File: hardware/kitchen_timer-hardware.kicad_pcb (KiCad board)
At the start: 2 copper layers, 60 x 110.8 mm, 80 parts, among them J1 Conn_01x02, J2 Conn_01x02_Pin, J3 AVR-ISP-6, Q1 JSM2302, Q2 IRLML6402, Q3 MMBT3904, SW2 SKRPACE010, U1 CH340E UART Module, U10 MAX7219, U11 KWM-20882CUYB, U12 KWM-20882CUYB, U13 KWM-20882CUYB, U14 KWM-20882CUYB, U2 TP4056 breakout, U3 SparkFun_LiPower, U5 ATMEGA328P-AU, U6 PEC11R-4215F-S0024, U7 MAX7219, U8 MAX7219, U9 MAX7219, Y1 Crystal-32kHz

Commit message: Add description text
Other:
- board text added: "Kitchen Timer V1 2025-05-12 Nicolas Perozzi, Erasmus Cedernaes"
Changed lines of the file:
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@@
 		(layer "User.1")
+	)
+	(gr_text "Kitchen Timer V1\n2025-05-12\nNicolas Perozzi, Erasmus Cedernaes"
+		(at 135.5744 64.7192 90)
+		(layer "B.SilkS")
+		(effects
+			(font
+				(size 1 1.016)
+				(thickness 0.195)
+				(bold yes)
+			)
+			(justify left bottom mirror)
+		)
 	)
 	(segment

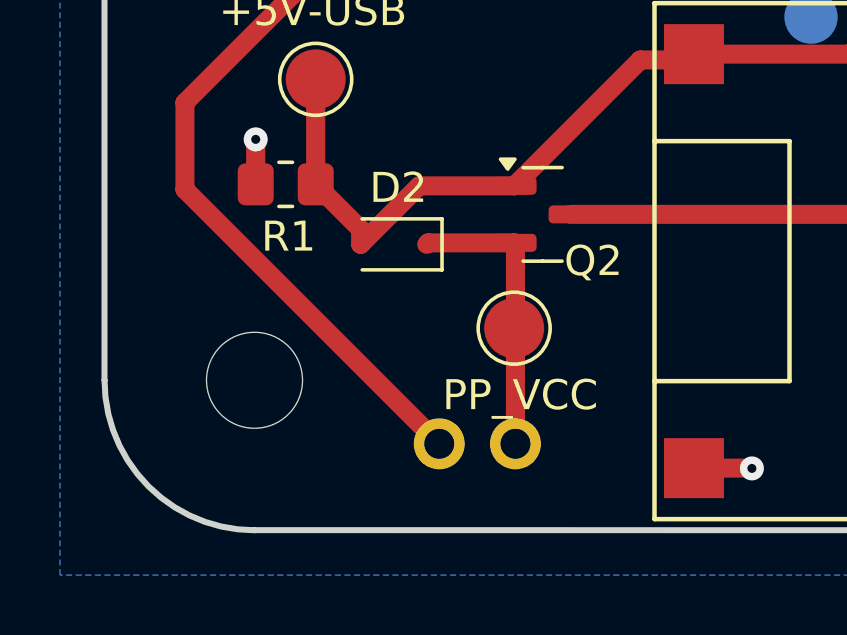
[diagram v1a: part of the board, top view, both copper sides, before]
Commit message: Move J2 connector further from the edge
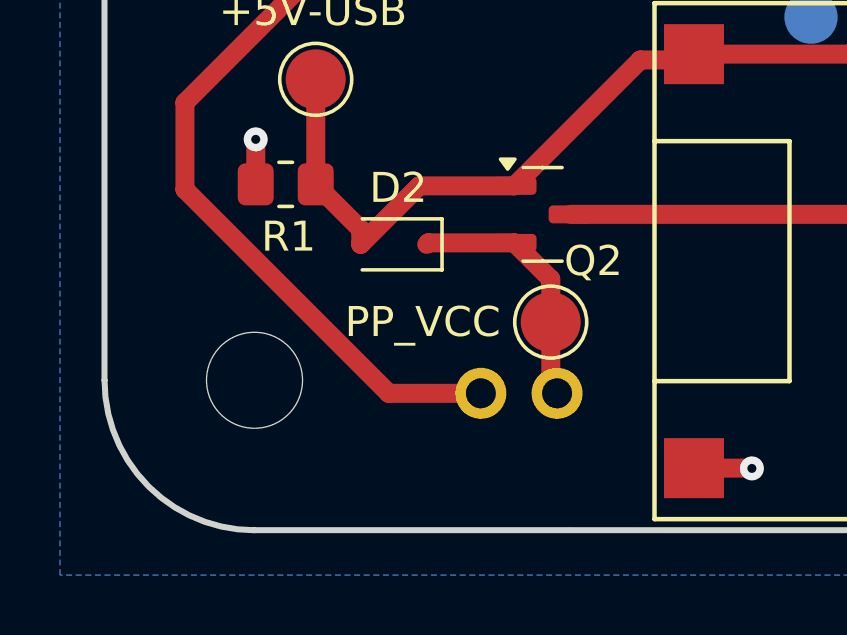
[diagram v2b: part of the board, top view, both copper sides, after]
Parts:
- moved J2 2.18 mm to (144.5, 136.4)
- moved TP13 1.24 mm to (141.9, 131.8)
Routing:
- net /+5V Boost Converter/PP_VCC: track 9.66 -> 8.55 mm
- net /+5V Boost Converter/PP_VCC_after_switch: track 25.8 -> 26.4 mm
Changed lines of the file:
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@@
 	(footprint "TestPoint:TestPoint_Pad_D2.0mm"
 		(layer "F.Cu")
-		(at 140.6544 131.9784)
+		(at 141.8736 131.7752)
 		(descr "SMD pad as test Point, diameter 2.0mm")
 		(tags "test point SMD pad")
@@
 		)
 		(property "Value" "PP_VCC"
-			(at 0.2032 2.2352 0)
+			(at -4.2672 0 0)
 			(layer "F.SilkS")
 			(effects
@@
 	(footprint "kitchen_timer:JST_XH_1x02_P2.54mm_Vertical"
 		(layer "B.Cu")
-		(at 143.1277 138.1321 180)
+		(at 144.5152 136.4488 180)
 		(descr "JST XH series connector, B2B-XH-AM, with boss (http://www.jst-mfg.com/product/pdf/eng/eXH.pdf), generated with kicad-footprint-generator")
 		(tags "connector JST XH vertical boss")
@@
 	)
 	(segment
-		(start 140.6977 129.1667)
+		(start 141.8736 133.9372)
+		(end 142.0852 134.1488)
+		(width 0.635)
+		(layer "F.Cu")
+		(net 12)
+	)
+	(segment
+		(start 141.8736 130.3426)
 		(end 140.665 129.134)
 		(width 0.635)
@@
 	)
 	(segment
-		(start 140.6977 135.8321)
-		(end 140.6977 129.1667)
+		(start 141.8736 131.7752)
+		(end 141.8736 130.3426)
 		(width 0.635)
 		(layer "F.Cu")
@@
 	)
 	(segment
+		(start 141.8736 131.7752)
+		(end 141.8736 133.9372)
+		(width 0.635)
+		(layer "F.Cu")
+		(net 12)
+	)
+	(segment
 		(start 140.665 129.134)
 		(end 137.79 129.134)
@@
 	)
 	(segment
+		(start 129.6816 124.46)
+		(end 136.9576 117.184)
+		(width 0.635)
+		(layer "F.Cu")
+		(net 22)
+	)
+	(segment
 		(start 136.9576 117.184)
 		(end 137.54 117.184)
@@
 	)
 	(segment
-		(start 129.6816 124.46)
-		(end 136.9576 117.184)
+		(start 139.5452 134.1488)
+		(end 136.4744 134.1488)
 		(width 0.635)
 		(layer "F.Cu")
@@
 	)
 	(segment
-		(start 138.1577 135.8321)
+		(start 136.4744 134.1488)
 		(end 129.6816 127.356)
 		(width 0.635)

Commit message: Run "cleanup tracks and vias"
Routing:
- net /LED Matrices Drivers/SCK: track 144.2 -> 143.1 mm
- net /Microcontroller/SW: track 12.0 -> 11.3 mm
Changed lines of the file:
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@@
 	)
 	(segment
-		(start 161.5775 76.184)
-		(end 161.54 76.184)
-		(width 0.2)
-		(layer "F.Cu")
-		(net 1)
-	)
-	(segment
 		(start 151.523 59.944)
 		(end 150.1032 59.944)
@@
 	(segment
 		(start 160.04 100.184)
-		(end 163.04 100.184)
+		(end 167.04 100.184)
 		(width 0.635)
 		(layer "F.Cu")
@@
 	(segment
 		(start 134.6854 77.184)
-		(end 134.6854 76.684)
+		(end 134.6854 74.8792)
 		(width 0.635)
 		(layer "F.Cu")
@@
 	(segment
 		(start 134.6854 97.3582)
-		(end 134.6854 89.184)
+		(end 134.6854 77.184)
 		(width 0.635)
 		(layer "F.Cu")
@@
 	)
 	(segment
-		(start 163.04 100.184)
-		(end 167.04 100.184)
-		(width 0.635)
-		(layer "F.Cu")
-		(net 2)
-	)
-	(segment
 		(start 137.54 89.184)
 		(end 139.54 87.184)
@@
 	)
 	(segment
-		(start 142.54 98.184)
-		(end 145.04 98.184)
+		(start 142.04 98.184)
+		(end 150.04 98.184)
 		(width 0.635)
 		(layer "F.Cu")
@@
 	)
 	(segment
-		(start 142.04 98.184)
-		(end 142.54 98.184)
-		(width 0.635)
-		(layer "F.Cu")
-		(net 2)
-	)
-	(segment
 		(start 135.7776 53.34)
 		(end 134.6865 52.2489)
@@
 	)
 	(segment
-		(start 134.6854 75.684)
-		(end 134.6854 74.8792)
-		(width 0.635)
-		(layer "F.Cu")
-		(net 2)
-	)
-	(segment
 		(start 158.0025 89.1465)
 		(end 158.54 89.1465)
@@
 	)
 	(segment
-		(start 134.6854 89.184)
-		(end 134.6854 77.184)
-		(width 0.635)
-		(layer "F.Cu")
-		(net 2)
-	)
-	(segment
 		(start 173.8024 109.4952)
 		(end 171.5248 109.4952)
@@
 	)
 	(segment
-		(start 159.5935 78.3917)
-		(end 159.54 78.4452)
-		(width 0.2)
-		(layer "F.Cu")
-		(net 2)
-	)
-	(segment
-		(start 134.6854 76.684)
-		(end 134.6854 75.684)
-		(width 0.635)
-		(layer "F.Cu")
-		(net 2)
-	)
-	(segment
 		(start 135.93 64.008)
 		(end 136.184 63.754)
@@
 	)
 	(segment
-		(start 145.04 98.184)
-		(end 150.04 98.184)
-		(width 0.635)
-		(layer "F.Cu")
-		(net 2)
-	)
-	(segment
 		(start 158.74 88.9465)
 		(end 158.54 89.1465)
@@
 	)
 	(segment
-		(start 142.54 85.1465)
+		(start 141.0775 85.1465)
 		(end 144.5775 85.1465)
 		(width 0.2)
@@
 		(net 5)
 	)
-	(segment
-		(start 141.0775 85.1465)
-		(end 142.54 85.1465)
-		(width 0.2)
-		(layer "F.Cu")
-		(net 5)
-	)
 	(via
 		(at 161.4824 86.5632)
@@
 	)
 	(segment
-		(start 157.54 93.684)
-		(end 157.04 93.184)
-		(width 0.2)
-		(layer "F.Cu")
-		(net 7)
-	)
-	(segment
 		(start 157.04 90.6465)
 		(end 155.54 89.1465)
@@
 	)
 	(segment
-		(start 146.54 97.835)
-		(end 146.54 97.184)
-		(width 0.2)
-		(layer "B.Cu")
-		(net 8)
-	)
-	(segment
 		(start 146.54 99.184)
-		(end 146.54 97.835)
+		(end 146.54 97.184)
 		(width 0.2)
 		(layer "B.Cu")
@@
 	)
 	(segment
-		(start 161.544 116.4105)
-		(end 161.544 116.188)
-		(width 0.2)
-		(layer "F.Cu")
-		(net 10)
-	)
-	(segment
 		(start 140.54 113.7792)
 		(end 143.7024 116.9416)
@@
 	)
 	(segment
-		(start 140.536592 99.1015)
-		(end 140.54 99.104908)
-		(width 0.2)
-		(layer "F.Cu")
-		(net 10)
-	)
-	(segment
 		(start 161.544 116.4105)
 		(end 161.8135 116.4105)
@@
 	)
 	(segment
-		(start 155.555525 121.684)
-		(end 155.54 121.684)
-		(width 0.2)
-		(layer "F.Cu")
-		(net 11)
-	)
-	(segment
-		(start 155.630125 121.6094)
-		(end 155.555525 121.684)
-		(width 0.2)
-		(layer "F.Cu")
-		(net 11)
-	)
-	(segment
 		(start 160.594 118.2855)
 		(end 159.3488 119.5307)
@@
 		(net 11)
 	)
-	(segment
-		(start 155.630125 121.6094)
-		(end 155.640329 121.599196)
-		(width 0.2)
-		(layer "F.Cu")
-		(net 11)
-	)
 	(via
 		(at 155.630125 121.6094)
@@
 		(net 13)
 	)
-	(segment
-		(start 153.04 121.659525)
-		(end 153.090125 121.6094)
-		(width 0.635)
-		(layer "F.Cu")
-		(net 13)
-	)
 	(via
 		(at 153.090125 121.6094)
@@
 		(net 23)
 	)
-	(segment
-		(start 161.79 80.6952)
-		(end 161.893124 80.592076)
-		(width 0.2)
-		(layer "F.Cu")
-		(net 23)
-	)
 	(via
 		(at 170.728 78.4194)
@@
 	)
 	(segment
-		(start 162.04 78.4452)
+		(start 160.34 78.4452)
 		(end 162.2788 78.4452)
 		(width 0.254)
@@
 	)
 	(segment
-		(start 160.34 78.4452)
-		(end 162.04 78.4452)
-		(width 0.254)
-		(layer "F.Cu")
-		(net 24)
-	)
-	(segment
 		(start 147.5968 36.508)
 		(end 146.9688 35.88)
@@
 	)
 	(segment
-		(start 176.651 81.295)
-		(end 177.2704 81.295)
-		(width 0.254)
-		(layer "F.Cu")
-		(net 24)
-	)
-	(segment
 		(start 137.588 37.377757)
 		(end 137.588 37.971615)
@@
 	)
 	(segment
-		(start 156.7072 56.1848)
-		(end 156.312 56.1848)
-		(width 0.254)
-		(layer "F.Cu")
-		(net 24)
-	)
-	(segment
 		(start 162.2788 78.4452)
 		(end 164.4288 78.4452)
@@
 	)
 	(segment
-		(start 141.540003 97.231203)
-		(end 141.54 97.2312)
-		(width 0.2)
-		(layer "F.Cu")
-		(net 28)
-	)
-	(segment
-		(start 153.3012 84.684)
-		(end 153.29 84.6952)
-		(width 0.2)
-		(layer "F.Cu")
-		(net 28)
-	)
-	(segment
 		(start 141.54 94.184)
 		(end 151.0288 84.6952)
@@
 	)
 	(segment
-		(start 141.536594 99.101499)
-		(end 141.54 99.104905)
-		(width 0.2)
-		(layer "F.Cu")
-		(net 28)
-	)
-	(segment
 		(start 151.0288 84.6952)
 		(end 153.29 84.6952)
@@
 	)
 	(segment
-		(start 172.1025 91.234)
-		(end 172.05602 91.18752)
-		(width 0.2)
-		(layer "F.Cu")
-		(net 29)
-	)
-	(segment
 		(start 174.3856 76.0984)
 		(end 175.6256 76.0984)
@@
 	)
 	(segment
-		(start 169.458 109.4284)
-		(end 169.5248 109.4952)
-		(width 0.2)
-		(layer "F.Cu")
-		(net 33)
-	)
-	(segment
 		(start 159.5 112.6952)
 		(end 166.242 112.6952)
@@
 		(net 90)
 	)
-	(segment
-		(start 165.9499 38.505)
-		(end 165.9485 38.5064)
-		(width 0.254)
-		(layer "B.Cu")
-		(net 90)
-	)
